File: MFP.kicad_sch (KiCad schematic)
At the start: 5 parts, among them J2 Conn_01x06, J3 Conn_01x05, U2 MC68901, X2 7.3728 MHz

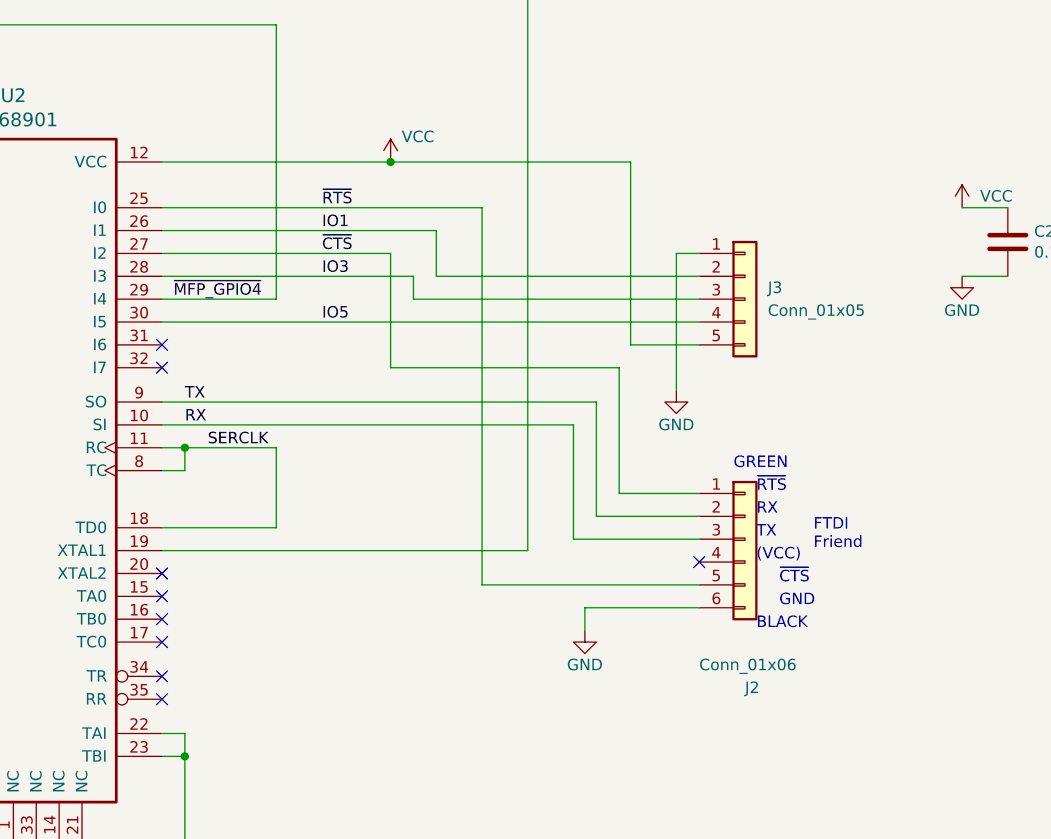
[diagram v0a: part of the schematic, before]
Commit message: V1C version of BITSY that uses an SRAM SIMM for memory.
This version sent to JLCPCB on 08/15/2025.
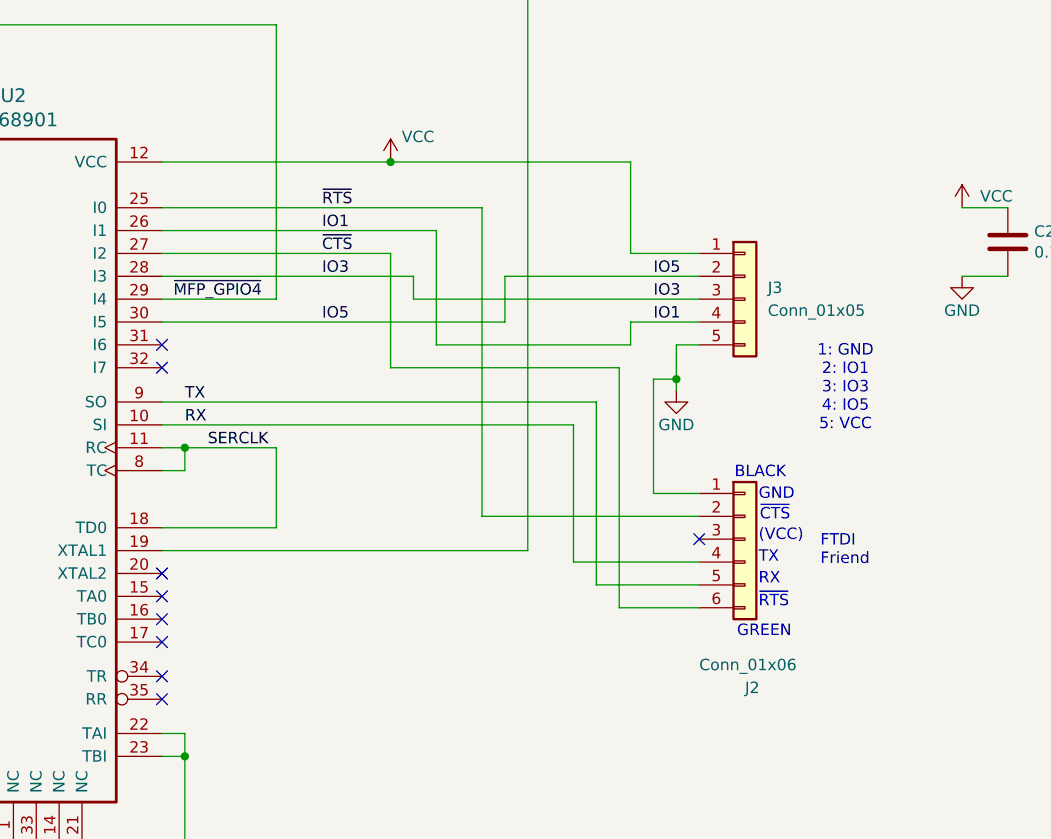
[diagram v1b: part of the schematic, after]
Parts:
- J2: footprint Connector_PinHeader_2.54mm:PinHeader_1x06_P2.54mm_Vertical -> Connector_PinHeader_2.54mm:PinHeader_1x06_P2.54mm_Horizontal
- J3: footprint Connector_PinHeader_2.54mm:PinHeader_1x05_P2.54mm_Vertical -> Connector_PinHeader_2.54mm:PinHeader_1x05_P2.54mm_Horizontal
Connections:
- net GND: now also J2.1 (Pin_1), J3.5 (Pin_5); no longer J2.6 (Pin_6), J3.1 (Pin_1)
- net IO1: now also J3.4 (Pin_4); no longer J3.2 (Pin_2)
- net IO5: now also J3.2 (Pin_2); no longer J3.4 (Pin_4)
- net RX: now also J2.4 (Pin_4); no longer J2.3 (Pin_3)
- net TX: now also J2.5 (Pin_5); no longer J2.2 (Pin_2)
- net VCC: now also J3.1 (Pin_1); no longer J3.5 (Pin_5)
- net ~{CTS}: now also J2.6 (Pin_6); no longer J2.1 (Pin_1)
- net ~{RTS}: now also J2.2 (Pin_2); no longer J2.5 (Pin_5)
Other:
- note added: "1: GND 2: IO1 3: IO3 4: IO5 5: VCC"
